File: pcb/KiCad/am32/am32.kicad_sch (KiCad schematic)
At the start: 62 parts, among them IC1 STM32G071CBU6, Q1 TPHR8504PL_L1Q, Q2 TPHR8504PL_L1Q, Q3 TPHR8504PL_L1Q, Q4 TPHR8504PL_L1Q, Q5 TPHR8504PL_L1Q, Q6 TPHR8504PL_L1Q, U1 TS3480CX33 RFG, U4 INA180B3IDBVR

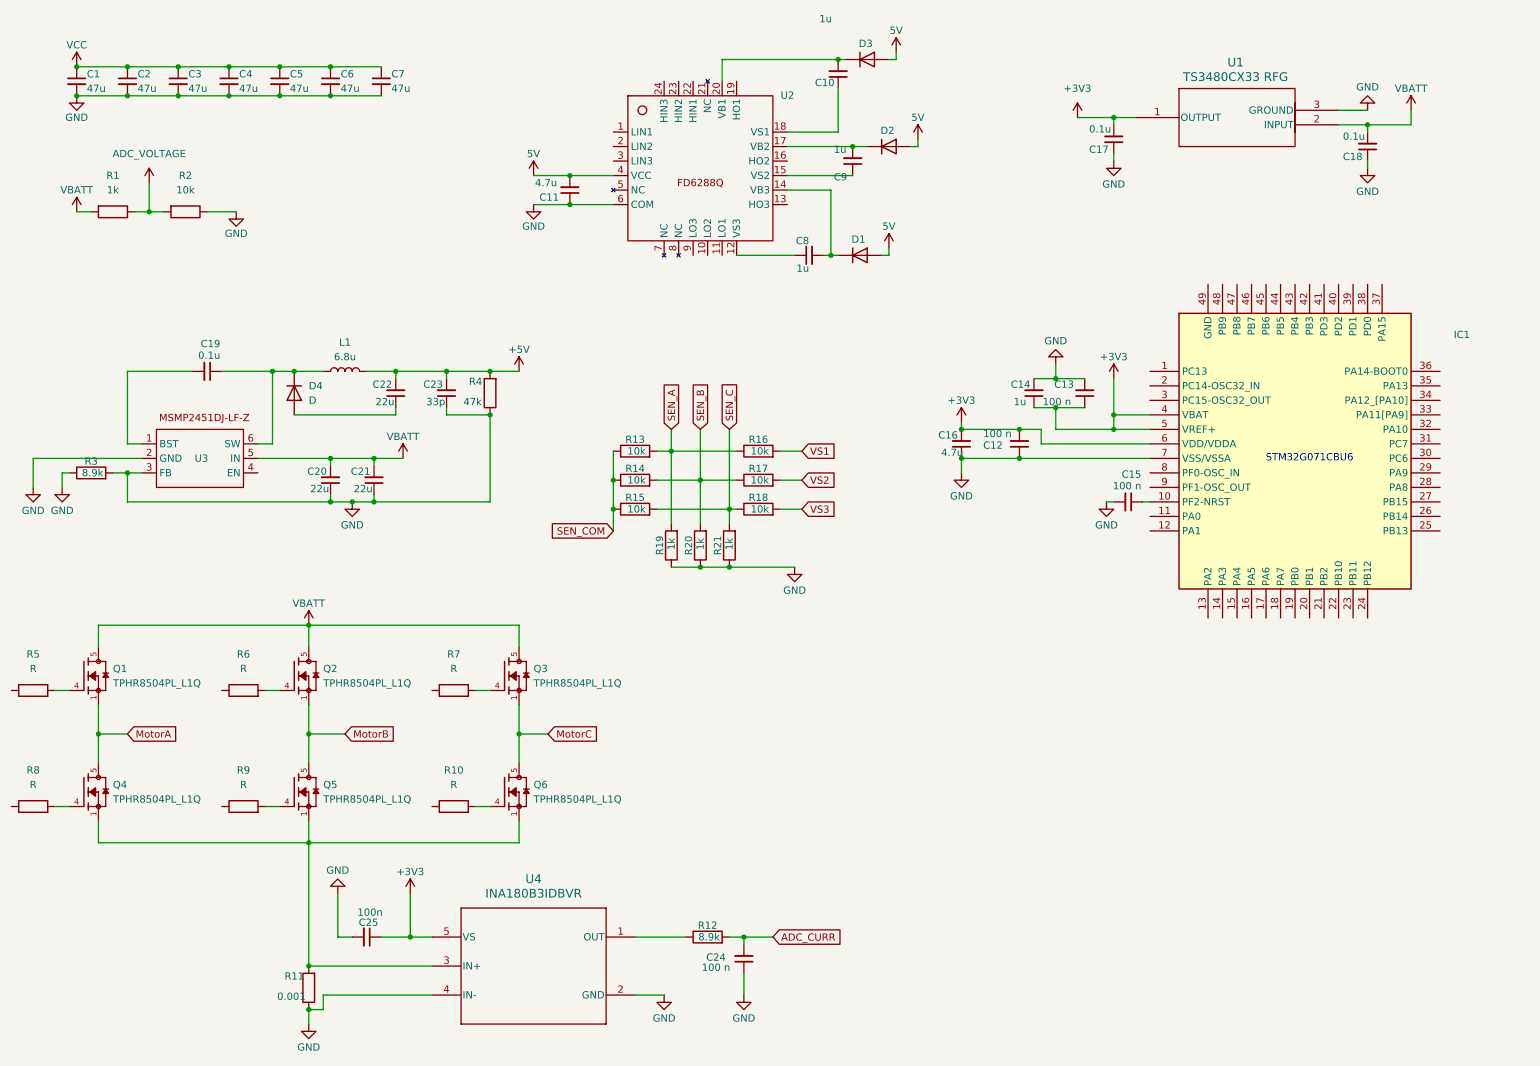
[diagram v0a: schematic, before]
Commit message: Added labels to KiCad project
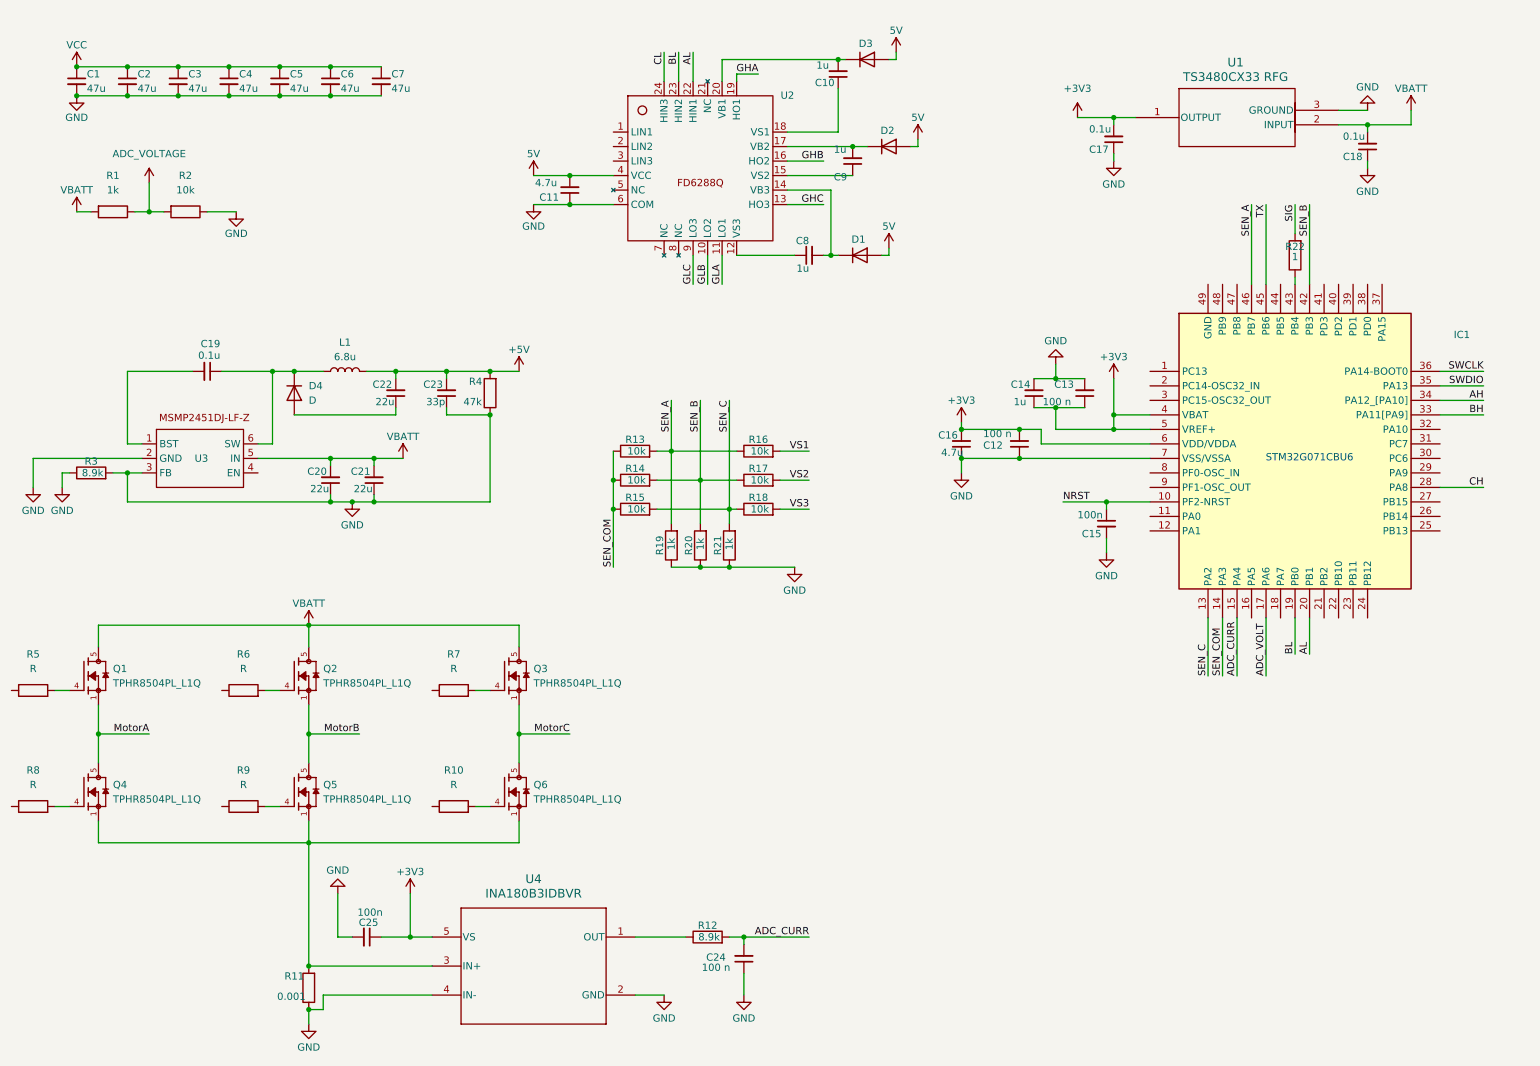
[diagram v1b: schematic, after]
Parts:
- added R22: 1, symbol Device:R
- C15: value 100 n -> 100n
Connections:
- net ADC_CURR: now also IC1.15 (PA4)
- net SEN_A: now also IC1.46 (PB7)
- net SEN_B: now also IC1.42 (PB3)
- net SEN_C: now also IC1.13 (PA2)
- net SEN_COM: now also IC1.14 (PA3)
- net NRST: now reaches C15.1, IC1.10 (PF2-NRST)
- net GLB: now reaches U2.10 (LO2)
- net GLA: now reaches U2.11 (LO1)
- net GHC: now reaches U2.13 (HO3)
- net GHB: now reaches U2.16 (HO2)
- net GHA: now reaches U2.19 (HO1)
- net AL: now reaches U2.22 (HIN1)
- net AL: now also IC1.20 (PB1)
- net BL: now reaches U2.23 (HIN2)
- net BL: now also IC1.19 (PB0)
- net CL: now reaches U2.24 (HIN3)
- net GLC: now reaches U2.9 (LO3)
- net ADC_VOLT: now reaches IC1.17 (PA6)
- net CH: now reaches IC1.28 (PA8)
- net BH: now reaches IC1.33 (PA11[PA9])
- net AH: now reaches IC1.34 (PA12_[PA10])
- net SWDIO: now reaches IC1.35 (PA13)
- net SWCLK: now reaches IC1.36 (PA14-BOOT0)
- net at IC1.43 (PB4): now also R22.1
- net TX: now reaches IC1.45 (PB6)
- new net SIG: R22.2
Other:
- moved on the sheet: C15

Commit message: Adding leftovers
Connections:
- net GHA: now also R5.1
- net GHB: now also R6.1
- net GHC: now also R7.1
- net GLA: now also R8.1
- net GLB: now also R9.1
- net GLC: now also R10.1
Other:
- moved on the sheet: C24, C25, Q1, Q2, Q3, Q4, Q5, Q6, R10, R11, R12, R5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

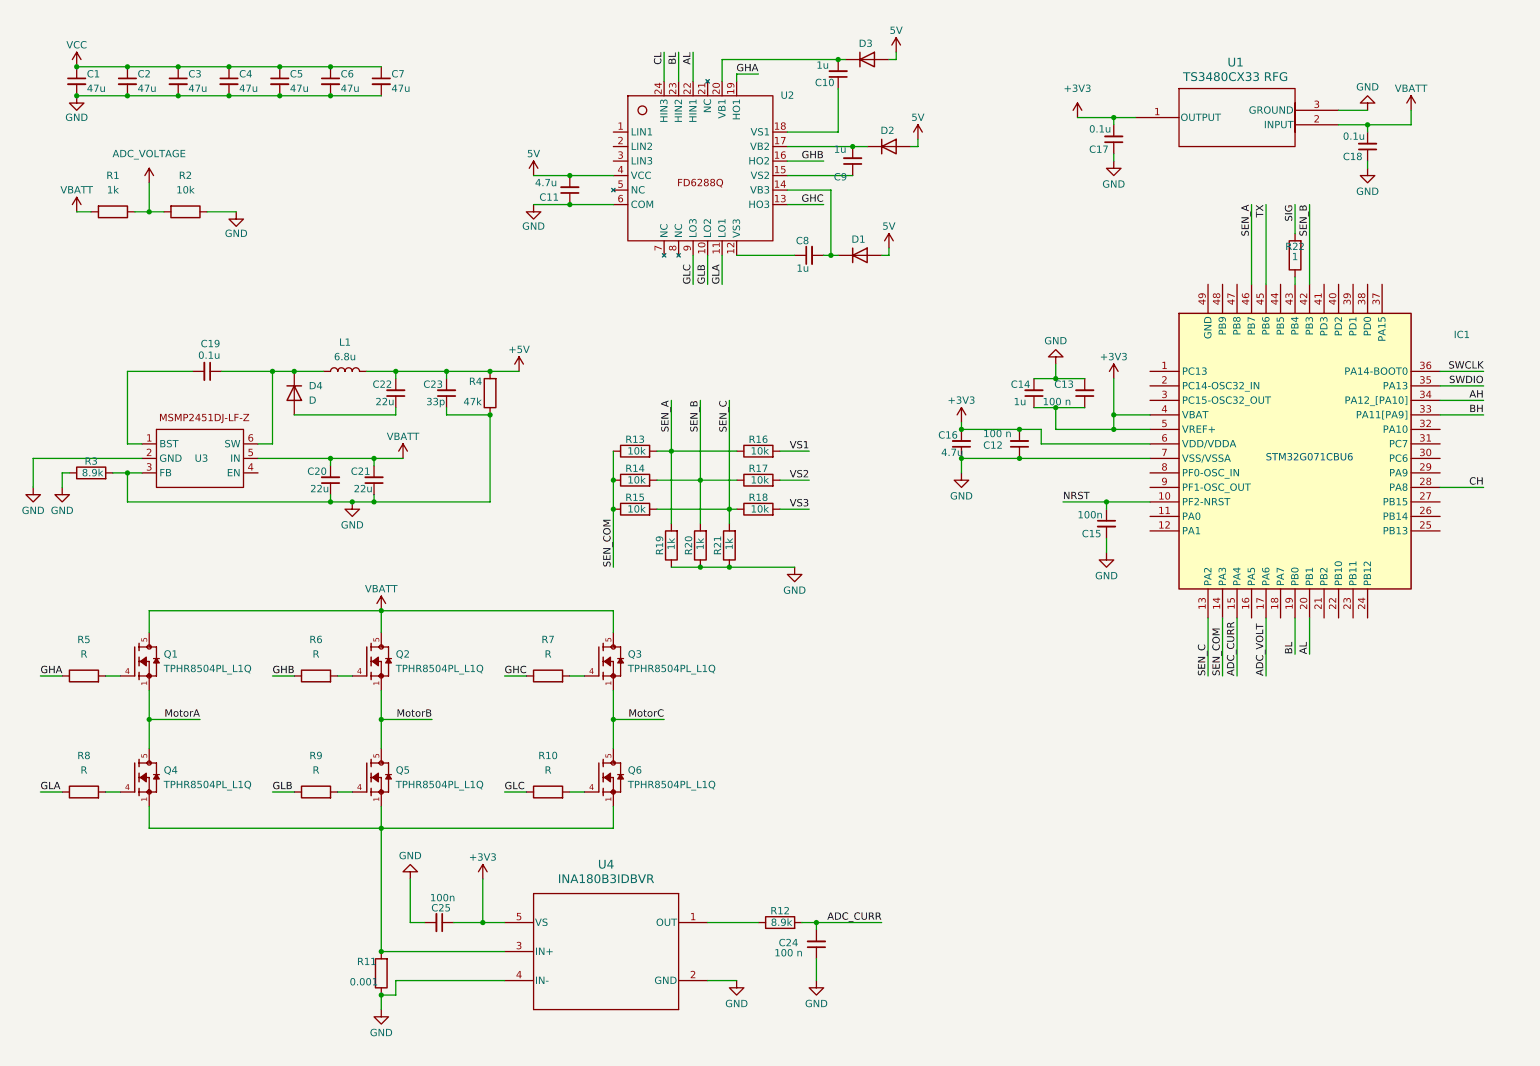
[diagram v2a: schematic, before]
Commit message: used right stm32 layout
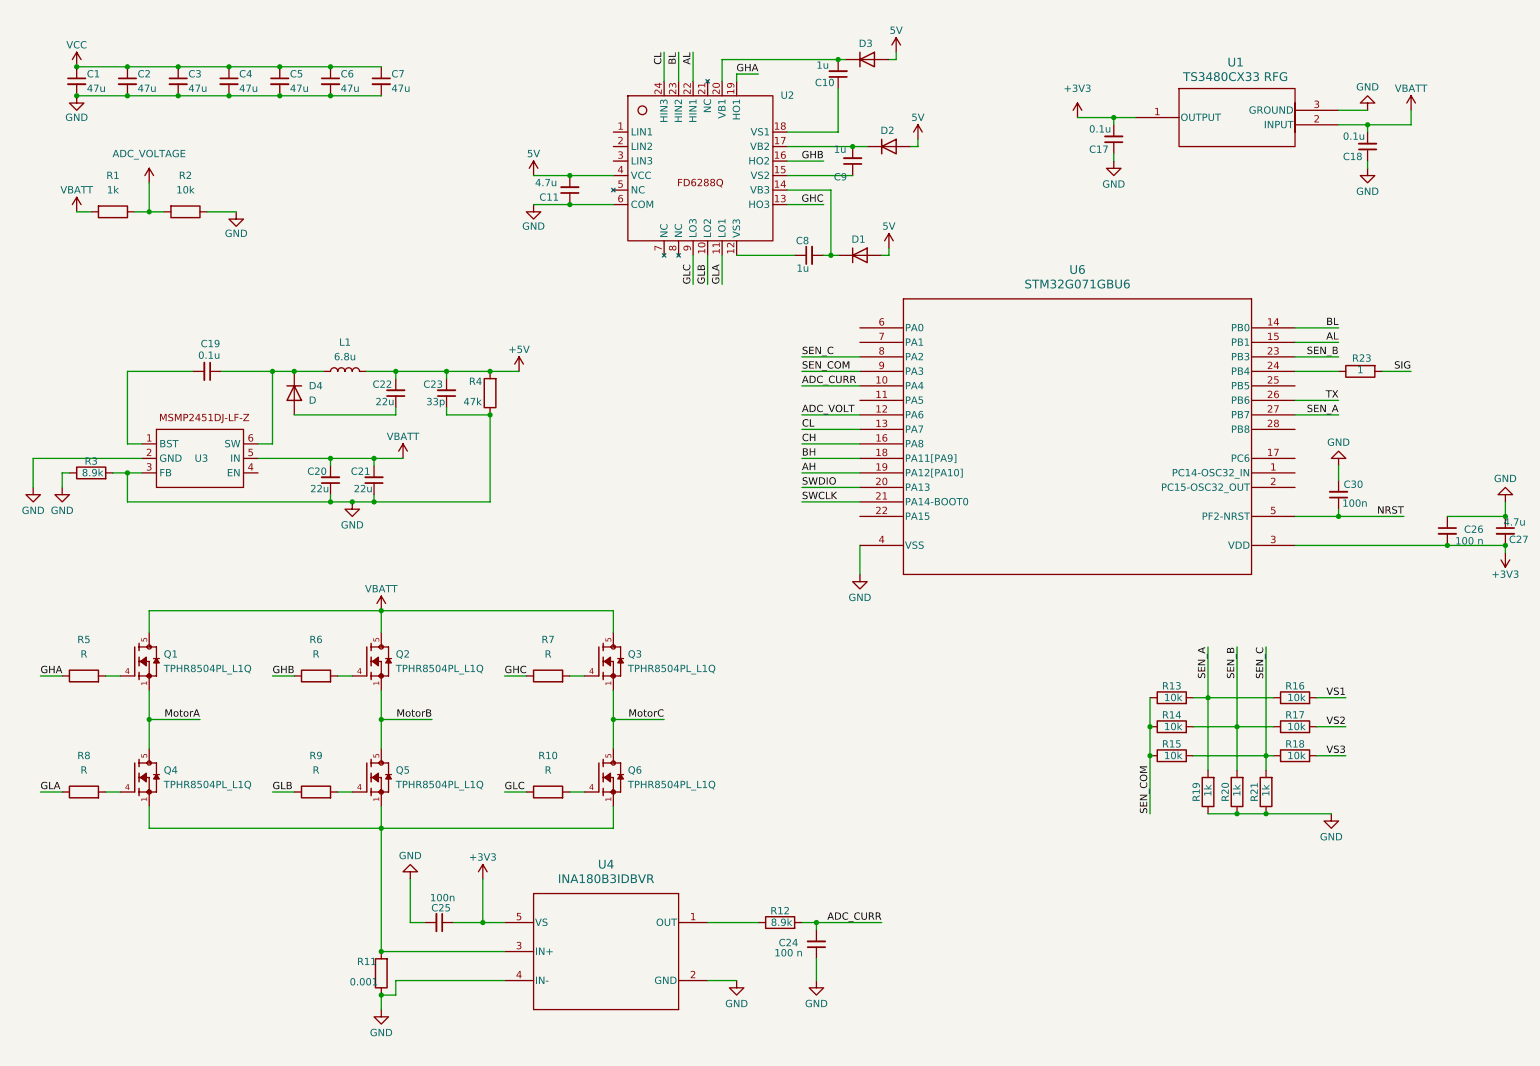
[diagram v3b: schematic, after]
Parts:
- removed C12, C13: 100 n, PCM_SparkFun-Capacitor:C_0603_1608Metric, symbol PCM_SparkFun-Capacitor:C
- removed C14: 1u, PCM_SparkFun-Capacitor:C_0603_1608Metric, symbol PCM_SparkFun-Capacitor:C
- removed C15: 100n, PCM_SparkFun-Capacitor:C_0603_1608Metric, symbol PCM_SparkFun-Capacitor:C
- removed C16: 4.7u, PCM_SparkFun-Capacitor:C_0603_1608Metric, symbol PCM_SparkFun-Capacitor:C
- removed IC1: STM32G071CBU6, QFN50P700X700X60-49N-D, symbol STM32G071CBU6:STM32G071CBU6
- removed R22: 1, symbol Device:R
- added C26: 100 n, PCM_SparkFun-Capacitor:C_0603_1608Metric, symbol PCM_SparkFun-Capacitor:C
- added C27: 4.7u, PCM_SparkFun-Capacitor:C_0603_1608Metric, symbol PCM_SparkFun-Capacitor:C
- added C30: 100n, PCM_SparkFun-Capacitor:C_0603_1608Metric, symbol PCM_SparkFun-Capacitor:C
- added R23: 1, symbol Device:R
- added U6: STM32G071GBU6, UFQFPN-28, symbol 2026-02-15_08-47-09:STM32G071GBU6
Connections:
- net +3V3: now also C26.2, C27.2, U6.3 (VDD)
- net ADC_CURR: now also U6.10 (PA4)
- net ADC_VOLT: now also U6.12 (PA6)
- net AH: now also U6.19 (PA12[PA10])
- net AL: now also U6.15 (PB1)
- net BH: now also U6.18 (PA11[PA9])
- net BL: now also U6.14 (PB0)
- net CH: now also U6.16 (PA8)
- net CL: now also U6.13 (PA7)
- net GND: now also C26.1, C27.1, C30.2, U6.4 (VSS)
- net NRST: now also C30.1, U6.5 (PF2-NRST)
- net SEN_A: now also U6.27 (PB7)
- net SEN_B: now also U6.23 (PB3)
- net SEN_C: now also U6.8 (PA2)
- net SEN_COM: now also U6.9 (PA3)
- net SIG: now also R23.2
- net SWCLK: now also U6.21 (PA14-BOOT0)
- net SWDIO: now also U6.20 (PA13)
- net TX: now also U6.26 (PB6)
- new net: R23.1, U6.24 (PB4)
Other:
- note removed: "STM32G071CBU6"
- moved on the sheet: R13, R14, R15, R16, R17, R18, R19, R20, R21
